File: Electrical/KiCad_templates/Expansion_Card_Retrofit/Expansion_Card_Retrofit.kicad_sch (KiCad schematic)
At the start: 19 parts, among them J1 Conn 10P, P1 USB_C_Plug_USB2.0, SW1 SW_DIP_x01, U1 AP2112K-3.3, X1 12MHz

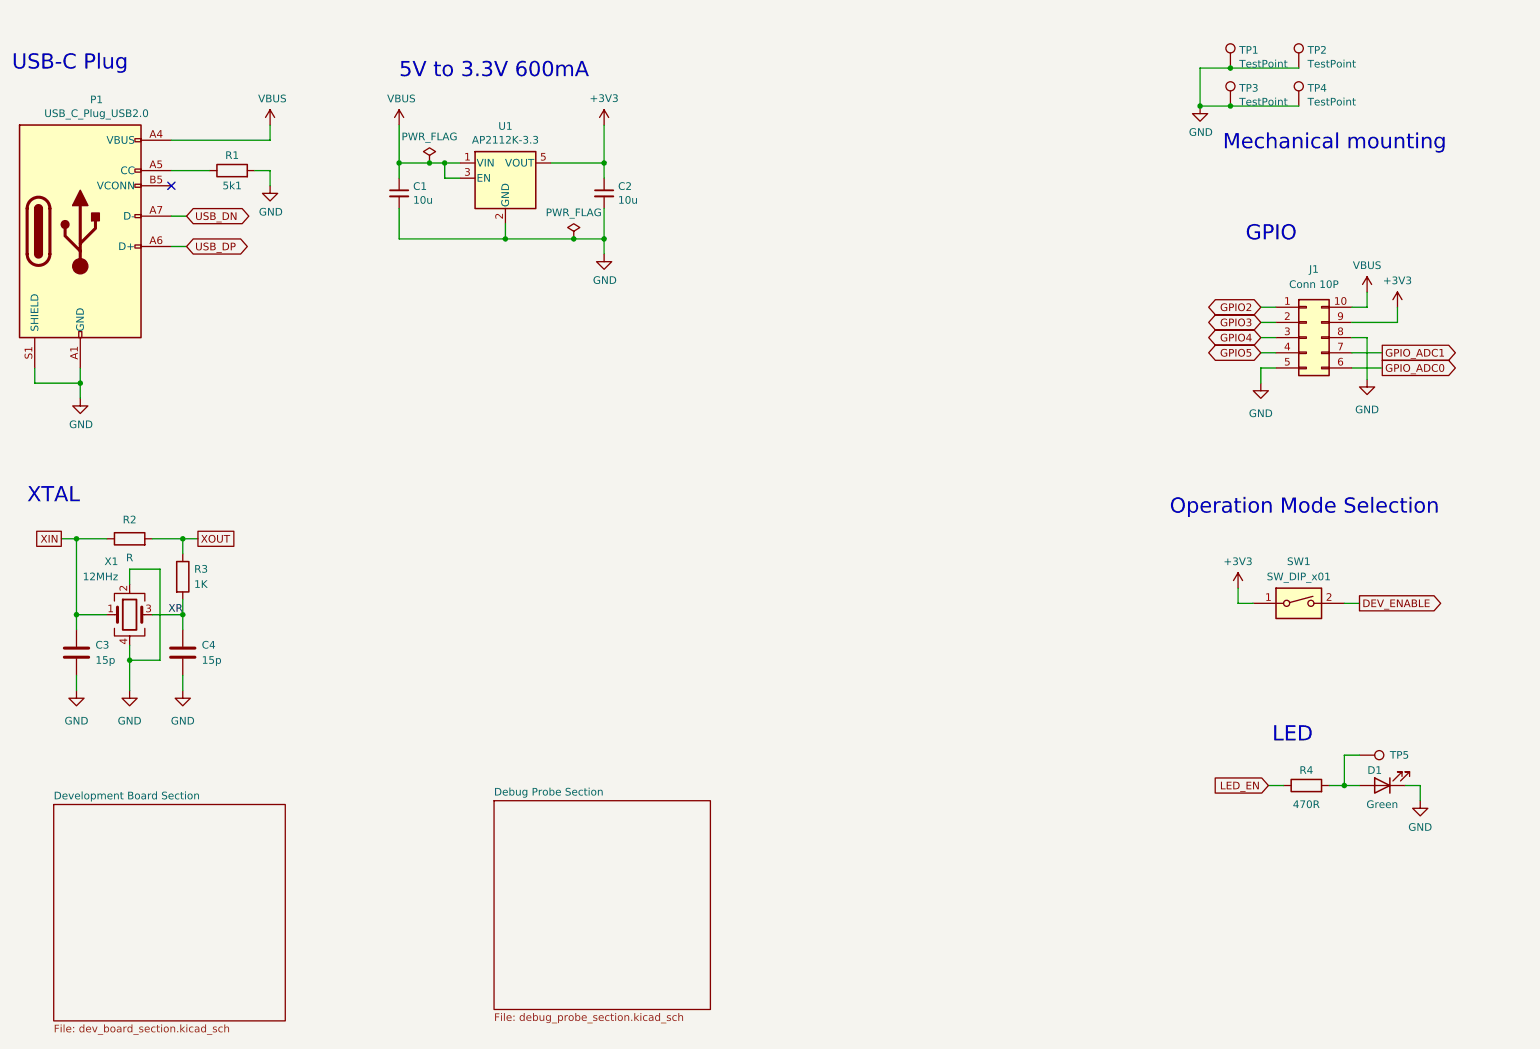
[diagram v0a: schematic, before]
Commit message: Main layout of chip sections finished
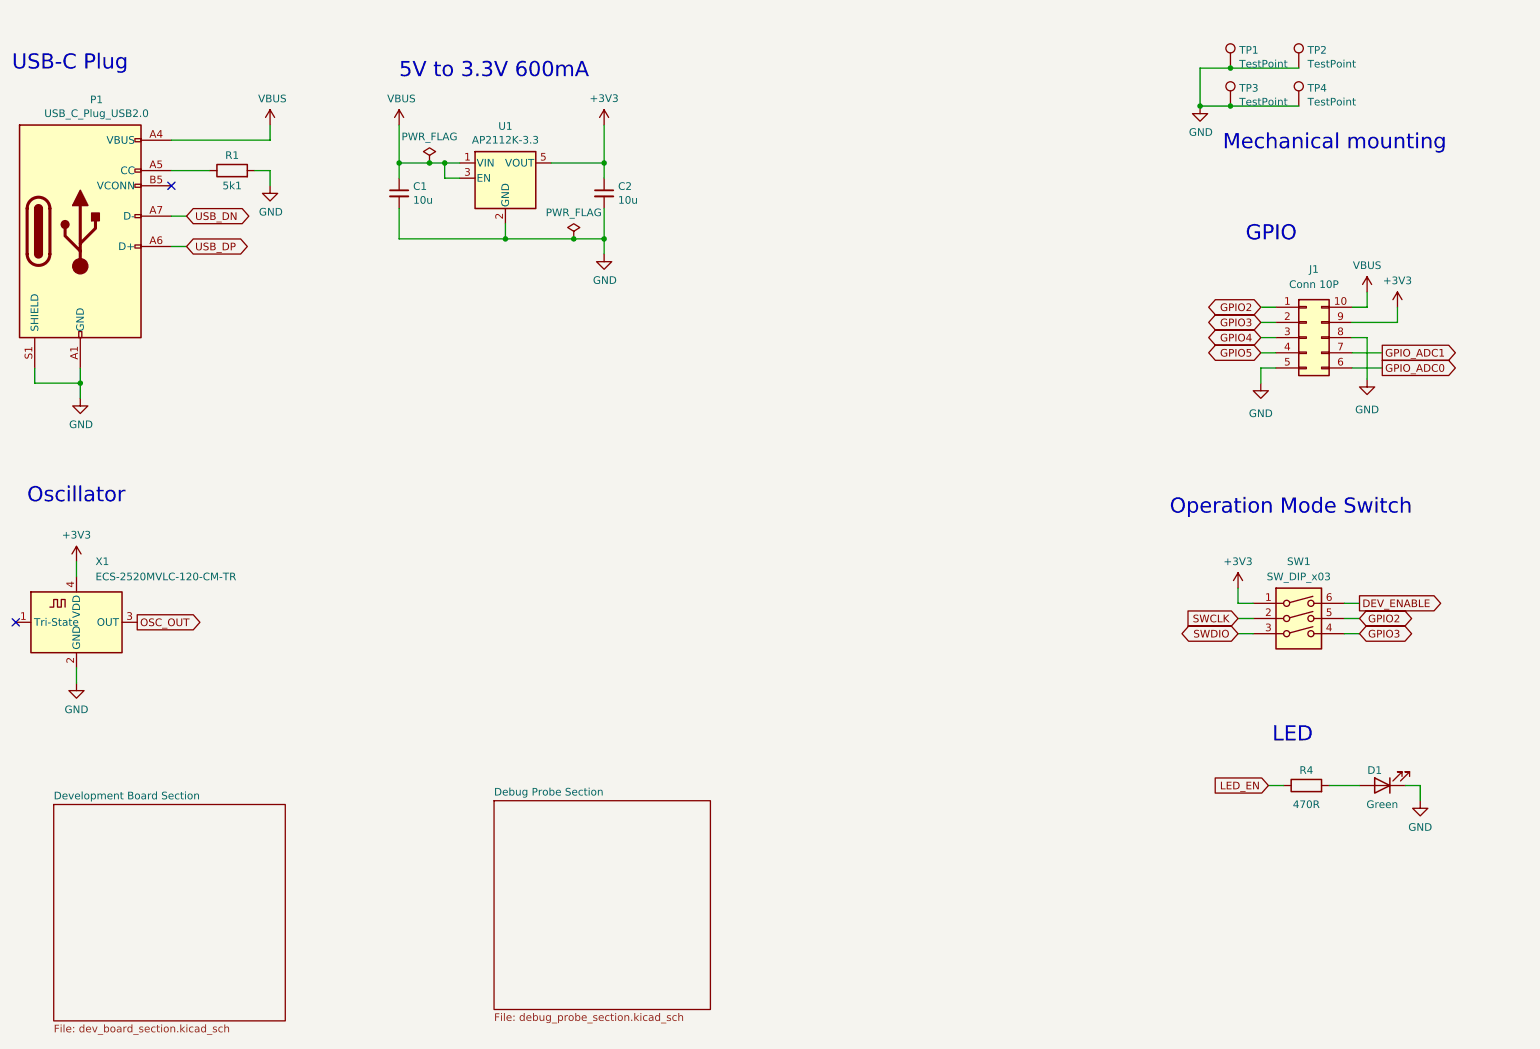
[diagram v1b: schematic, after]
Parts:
- removed C3, C4: 15p, Capacitor_SMD:C_0201_0603Metric, symbol Device:C
- removed R2: R, Resistor_SMD:R_0402_1005Metric, symbol Device:R
- removed R3: 1K, Resistor_SMD:R_0402_1005Metric, symbol Device:R
- removed SW1: SW_DIP_x01, symbol Switch:SW_DIP_x01
- removed TP5: TestPoint, TestPoint:TestPoint_Pad_1.5x1.5mm, symbol Connector:TestPoint
- removed X1: 12MHz, Crystal:Crystal_SMD_0603-4Pin_6.0x3.5mm, symbol Device:Crystal_GND24
- added SW1: SW_DIP_x03, symbol Switch:SW_DIP_x03
- added X1: ECS-2520MVLC-120-CM-TR, Oscillator:Oscillator_SMD_ECS_2520MV-xxx-xx-4Pin_2.5x2.0mm, symbol Oscillator:ECS-2520MV-xxx-xx
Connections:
- net +3V3: now also SW1.1, X1.4 (VDD)
- net DEV_ENABLE: now also SW1.6
- net GND: now also X1.2 (GND)
- net GPIO2: now also SW1.5
- net GPIO3: now also SW1.4
- new net OSC_OUT: X1.3 (OUT)
- new net SWCLK: SW1.2
- new net SWDIO: SW1.3
- no-connect marks 1 -> 2
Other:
- note added: "Operation Mode Switch"
- note added: "Oscillator"
- note removed: "Operation Mode Selection"
- note removed: "XTAL"

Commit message: Current state before flash footprint update
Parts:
- J1: footprint Connector_PinSocket_2.54mm:PinSocket_2x05_P2.54mm_Horizontal -> SnapEDA:AMPHENOL_89883-405LF; symbol Connector_Generic:Conn_02x05_Counter_Clockwise -> Connector_Generic:Conn_02x05_Odd_Even
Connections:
- net +3V3: now also J1.2 (Pin_2); no longer J1.9 (Pin_9)
- net GND: now also J1.3 (Pin_3), J1.9 (Pin_9); no longer J1.5 (Pin_5), J1.8 (Pin_8)
- net GPIO2: now also J1.4 (Pin_4); no longer J1.1 (Pin_1)
- net GPIO3: now also J1.6 (Pin_6); no longer J1.2 (Pin_2)
- net GPIO4: now also J1.8 (Pin_8); no longer J1.3 (Pin_3)
- net GPIO5: now also J1.10 (Pin_10); no longer J1.4 (Pin_4)
- net GPIO_ADC0: now also J1.7 (Pin_7); no longer J1.6 (Pin_6)
- net GPIO_ADC1: now also J1.5 (Pin_5); no longer J1.7 (Pin_7)
- net VBUS: now also J1.1 (Pin_1); no longer J1.10 (Pin_10)

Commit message: First complete version
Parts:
- removed SW1: SW_DIP_x03, symbol Switch:SW_DIP_x03
- added Q3: Q_Dual_NPN_NPN_C2E2C1E1B1B2, digikey-footprints:SOT-363, symbol Device:Q_Dual_NPN_NPN_C2E2C1E1B1B2
- added S1: JS102011SAQN, SnapEDA:SW_JS102011SAQN, symbol SnapEDA:JS102011SAQN
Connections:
- net +3V3: now also S1.1
- net DEV_ENABLE: now also Q3.5 (B1), Q3.6 (B2), S1.2
- net GPIO2: now also Q3.2 (E2)
- net GPIO3: now also Q3.4 (E1)
- net SWCLK: now also Q3.1 (C2)
- net SWDIO: now also Q3.3 (C1)
- no-connect marks 2 -> 3
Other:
- moved on the sheet: D1, J1, R4, TP1, TP2, TP3, TP4

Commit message: All footprints placed single-sided
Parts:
- C1, C2: footprint Capacitor_SMD:C_0603_1608Metric -> Capacitor_SMD:C_0402_1005Metric
- U1: value AP2112K-3.3 -> AP7366EA-3.3; footprint Package_TO_SOT_SMD:SOT-23-5 -> Package_DFN_QFN:Diodes_UDFN2020-6_Type-F; symbol Regulator_Linear:AP2112K-3.3 -> Regulator_Linear:AP7366EA-3.3
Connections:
- net +3V3: now also U1.4 (VOUT); no longer U1.5 (VOUT)
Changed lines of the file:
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@@
     )
   )
-  (symbol (lib_id "Regulator_Linear:AP2112K-3.3") (at 113.03 44.45 0) (unit 1)
+  (symbol (lib_id "Regulator_Linear:AP7366EA-3.3") (at 113.03 44.45 0) (unit 1)
     (in_bom yes) (on_board yes) (dnp no)
     (property "Reference" "U1" (at 113.03 35.7632 0)
       (effects (font (size 1.27 1.27)))
     )
-    (property "Value" "AP2112K-3.3" (at 113.03 38.0746 0)
+    (property "Value" "AP7366EA-3.3" (at 113.03 38.0746 0)
       (effects (font (size 1.27 1.27)))
     )
-    (property "Footprint" "Package_TO_SOT_SMD:SOT-23-5" (at 113.03 36.195 0)
+    (property "Footprint" "Package_DFN_QFN:Diodes_UDFN2020-6_Type-F" (at 113.03 36.195 0)
       (effects (font (size 1.27 1.27)) hide)
     )
-    (property "Datasheet" "https://www.diodes.com/assets/Datasheets/AP2112.pdf" (at 113.03 41.91 0)
+    (property "Datasheet" "https://www.diodes.com/assets/Datasheets/AP2204.pdf" (at 113.03 41.91 0)
       (effects (font (size 1.27 1.27)) hide)
     )
@@
     (pin "4")
     (pin "5")
+    (pin "6")
     (instances
       (project "Expansion_Card_Retrofit"
@@
       (effects (font (size 1.27 1.27)) (justify left))
     )
-    (property "Footprint" "Capacitor_SMD:C_0603_1608Metric" (at 95.25 46.99 0)
+    (property "Footprint" "Capacitor_SMD:C_0402_1005Metric" (at 95.25 46.99 0)
       (effects (font (size 1.27 1.27)) hide)
     )
@@
       (effects (font (size 1.27 1.27)) (justify left))
     )
-    (property "Footprint" "Capacitor_SMD:C_0603_1608Metric" (at 129.54 46.99 0)
+    (property "Footprint" "Capacitor_SMD:C_0402_1005Metric" (at 129.54 46.99 0)
       (effects (font (size 1.27 1.27)) hide)
     )

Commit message: Single layer basic layout finished
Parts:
- J1: footprint SnapEDA:AMPHENOL_89883-405LF -> SnapEDA:Pinheader_PCB_Edge_2x5_2.54mm
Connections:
- net USB_DN renamed USB_D_N
- net USB_DP renamed USB_D_P
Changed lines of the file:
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@@
     )
   )
-  (global_label "USB_DP" (shape bidirectional) (at 59.69 55.88 0) (fields_autoplaced)
-    (effects (font (size 1.27 1.27)) (justify left))
-    (property "Intersheetrefs" "${INTERSHEET_REFS}" (at 70.2911 55.88 0)
+  (global_label "USB_D_P" (shape bidirectional) (at 59.69 55.88 0) (fields_autoplaced)
+    (effects (font (size 1.27 1.27)) (justify left))
+    (property "Intersheetrefs" "${INTERSHEET_REFS}" (at 71.2587 55.88 0)
       (effects (font (size 1.27 1.27)) (justify left) hide)
     )
@@
     )
   )
-  (global_label "USB_DN" (shape bidirectional) (at 59.69 50.8 0) (fields_autoplaced)
-    (effects (font (size 1.27 1.27)) (justify left))
-    (property "Intersheetrefs" "${INTERSHEET_REFS}" (at 70.3516 50.8 0)
+  (global_label "USB_D_N" (shape bidirectional) (at 59.69 50.8 0) (fields_autoplaced)
+    (effects (font (size 1.27 1.27)) (justify left))
+    (property "Intersheetrefs" "${INTERSHEET_REFS}" (at 71.3192 50.8 0)
       (effects (font (size 1.27 1.27)) (justify left) hide)
     )
@@
       (effects (font (size 1.27 1.27)))
     )
-    (property "Footprint" "SnapEDA:AMPHENOL_89883-405LF" (at 244.475 63.5 0)
-      (effects (font (size 1.27 1.27)) hide)
-    )
+    (property "Footprint" "SnapEDA:Pinheader_PCB_Edge_2x5_2.54mm" (at 244.475 63.5 0)
+      (effects (font (size 1.27 1.27)) hide)
+    )

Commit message: Layout finished
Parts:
- S1: value JS102011SAQN -> Würth_450404015514; footprint SnapEDA:SW_JS102011SAQN -> SnapEDA:450404015514; symbol SnapEDA:JS102011SAQN -> SnapEDA:450404015514; Check_prices https://www.snapeda.com/parts/JS102011SAQN/C%2526K/view-par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 -> https://www.snapeda.com/parts/450404015514/Wurth+Electronic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; DATASHEET-URL (none) -> https://www.we-online.com/catalog/datasheet/450404015514.pdf; IR (none) -> 300mA; MF C&K -> Wurth Electronics; MP JS102011SAQN -> 450404015514; PACKAGING (none) -> Tape and Reel; PART-NUMBER (none) -> 450404015514; Purchase-URL (none) -> https://www.snapeda.com/api/url_track_click_mouser/?unipart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; QTY (none) -> 150; SnapEDA_Link https://www.snapeda.com/parts/JS102011SAQN/C%2526K/view-par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 -> https://www.snapeda.com/parts/450404015514/Wurth+Electronic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; VR (none) -> 5V(DC)
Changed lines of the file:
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@@
   (no_connect (at 57.15 45.72))
   (no_connect (at 31.115 118.745))
-  (no_connect (at 217.805 101.6))
+  (no_connect (at 222.885 101.6))
   (wire (pts (xy 241.935 154.94) (xy 247.015 154.94))
     (stroke (width 0) (type default))
@@
     (stroke (width 0) (type default))
   )
-  (wire (pts (xy 215.265 96.52) (xy 217.805 96.52))
+  (wire (pts (xy 220.345 96.52) (xy 222.885 96.52))
     (stroke (width 0) (type default))
   )
@@
     (stroke (width 0) (type default))
   )
-  (wire (pts (xy 215.265 93.98) (xy 215.265 96.52))
+  (wire (pts (xy 220.345 93.98) (xy 220.345 96.52))
     (stroke (width 0) (type default))
   )
@@
     )
   )
-  (symbol (lib_id "power:+3V3") (at 215.265 93.98 0) (unit 1)
+  (symbol (lib_id "power:+3V3") (at 220.345 93.98 0) (unit 1)
     (in_bom yes) (on_board yes) (dnp no) (fields_autoplaced)
-    (property "Reference" "#PWR014" (at 215.265 97.79 0)
-      (effects (font (size 1.27 1.27)) hide)
-    )
-    (property "Value" "+3V3" (at 215.265 89.535 0)
-      (effects (font (size 1.27 1.27)))
-    )
-    (property "Footprint" "" (at 215.265 93.98 0)
-      (effects (font (size 1.27 1.27)) hide)
-    )
-    (property "Datasheet" "" (at 215.265 93.98 0)
+    (property "Reference" "#PWR014" (at 220.345 97.79 0)
+      (effects (font (size 1.27 1.27)) hide)
+    )
+    (property "Value" "+3V3" (at 220.345 89.535 0)
+      (effects (font (size 1.27 1.27)))
+    )
+    (property "Footprint" "" (at 220.345 93.98 0)
+      (effects (font (size 1.27 1.27)) hide)
+    )
+    (property "Datasheet" "" (at 220.345 93.98 0)
       (effects (font (size 1.27 1.27)) hide)
     )
@@
     )
   )
-  (symbol (lib_id "SnapEDA:JS102011SAQN") (at 225.425 99.06 0) (unit 1)
-    (in_bom yes) (on_board yes) (dnp no) (fields_autoplaced)
-    (property "Reference" "S1" (at 225.425 91.44 0)
-      (effects (font (size 1.27 1.27)))
-    )
-    (property "Value" "JS102011SAQN" (at 225.425 93.98 0)
-      (effects (font (size 1.27 1.27)))
-    )
-    (property "Footprint" "SnapEDA:SW_JS102011SAQN" (at 225.425 99.06 0)
-      (effects (font (size 1.27 1.27)) (justify bottom) hide)
-    )
-    (property "Datasheet" "" (at 225.425 99.06 0)
-      (effects (font (size 1.27 1.27)) hide)
-    )
-    (property "MF" "C&K" (at 225.425 99.06 0)
-      (effects (font (size 1.27 1.27)) (justify bottom) hide)
-    )
-    (property "Description" "\nSwitch, Slide, SPDT, ON-ON, 300mA, 6VDC, Surface Mount, R/A, Gull Wing | C&K JS102011SAQN\n" (at 225.425 99.06 0)
-      (effects (font (size 1.27 1.27)) (justify bottom) hide)
-    )
-    (property "Package" "None" (at 225.425 99.06 0)
-      (effects (font (size 1.27 1.27)) (justify bottom) hide)
-    )
-    (property "Price" "None" (at 225.425 99.06 0)
-      (effects (font (size 1.27 1.27)) (justify bottom) hide)
-    )
-    (property "Check_prices" "https://www.snapeda.com/parts/JS102011SAQN/C%2526K/view-part/?ref=eda" (at 225.425 99.06 0)
-      (effects (font (size 1.27 1.27)) (justify bottom) hide)
-    )
-    (property "SnapEDA_Link" "https://www.snapeda.com/parts/JS102011SAQN/C%2526K/view-part/?ref=snap" (at 225.425 99.06 0)
-      (effects (font (size 1.27 1.27)) (justify bottom) hide)
-    )
-    (property "MP" "JS102011SAQN" (at 225.425 99.06 0)
-      (effects (font (size 1.27 1.27)) (justify bottom) hide)
-    )
-    (property "Availability" "In Stock" (at 225.425 99.06 0)
-      (effects (font (size 1.27 1.27)) (justify bottom) hide)
-    )
-    (property "MANUFACTURER" "C&K" (at 225.425 99.06 0)
-      (effects (font (size 1.27 1.27)) (justify bottom) hide)
-    )
+  (symbol (lib_id "SnapEDA:450404015514") (at 227.965 99.06 0) (mirror y) (unit 1)
+    (in_bom yes) (on_board yes) (dnp no)
+    (property "Reference" "S1" (at 223.52 90.17 0)
+      (effects (font (size 1.27 1.27)) (justify right))
+    )
+    (property "Value" "Würth_450404015514" (at 223.52 92.71 0)
+      (effects (font (size 1.27 1.27)) (justify right))
+    )
+    (property "Footprint" "SnapEDA:450404015514" (at 227.965 99.06 0)
+      (effects (font (size 1.27 1.27)) (justify bottom) hide)
+    )
+    (property "Datasheet" "" (at 227.965 99.06 0)
+      (effects (font (size 1.27 1.27)) hide)
+    )
+    (property "MF" "Wurth Electronics" (at 227.965 99.06 0)
+      (effects (font (size 1.27 1.27)) (justify bottom) hide)
+    )
+    (property "Description" "\nMINI SLIDE SWITCH 6.7 X 2.7 MM.\n" (at 227.965 99.06 0)
+      (effects (font (size 1.27 1.27)) (justify bottom) hide)
+    )
+    (property "Package" "None" (at 227.965 99.06 0)
+      (effects (font (size 1.27 1.27)) (justify bottom) hide)
+    )
+    (property "Price" "None" (at 227.965 99.06 0)
+      (effects (font (size 1.27 1.27)) (justify bottom) hide)
+    )
+    (property "Check_prices" "https://www.snapeda.com/parts/450404015514/Wurth+Electronics+Inc./view-part/?ref=eda" (at 227.965 99.06 0)
+      (effects (font (size 1.27 1.27)) (justify bottom) hide)
+    )
+    (property "SnapEDA_Link" "https://www.snapeda.com/parts/450404015514/Wurth+Electronics+Inc./view-part/?ref=snap" (at 227.965 99.06 0)
+      (effects (font (size 1.27 1.27)) (justify bottom) hide)
+    )
+    (property "MP" "450404015514" (at 227.965 99.06 0)
+      (effects (font (size 1.27 1.27)) (justify bottom) hide)
+    )
+    (property "Availability" "In Stock" (at 227.965 99.06 0)
+      (effects (font (size 1.27 1.27)) (justify bottom) hide)
+    )
+    (property "MANUFACTURER" "C&K" (at 227.965 99.06 0)
+      (effects (font (size 1.27 1.27)) (justify bottom) hide)
+    )
+    (property "IR" "300mA" (at 227.965 99.06 0)
+      (effects (font (size 1.27 1.27)) (justify bottom) hide)
+    )
+    (property "QTY" "150" (at 227.965 99.06 0)
+      (effects (font (size 1.27 1.27)) (justify bottom) hide)
+    )
+    (property "PACKAGING" "Tape and Reel" (at 227.965 99.06 0)
+      (effects (font (size 1.27 1.27)) (justify bottom) hide)
+    )
+    (property "VR" "5V(DC)" (at 227.965 99.06 0)
+      (effects (font (size 1.27 1.27)) (justify bottom) hide)
+    )
+    (property "DATASHEET-URL" "https://www.we-online.com/catalog/datasheet/450404015514.pdf" (at 227.965 99.06 0)
+      (effects (font (size 1.27 1.27)) (justify bottom) hide)
+    )
+    (property "Purchase-URL" "https://www.snapeda.com/api/url_track_click_mouser/?unipart_id=3611018&manufacturer=Wurth Electronics&part_name=450404015514&search_term=450404015514" (at 227.965 99.06 0)
+      (effects (font (size 1.27 1.27)) (justify bottom) hide)
+    )
+    (property "PART-NUMBER" "450404015514" (at 227.965 99.06 0)
+      (effects (font (size 1.27 1.27)) (justify bottom) hide)
+    )
